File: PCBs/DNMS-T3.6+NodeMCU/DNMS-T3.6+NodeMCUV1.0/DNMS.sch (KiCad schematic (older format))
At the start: 12 parts, among them J1 Conn_2Rows-07Pins, J2 Conn_01x02, J3 Conn_01x04, J4 Conn_01x05, U1 NodeMCU V2, U2 NodeMCU V3, U3 Teensy3.6

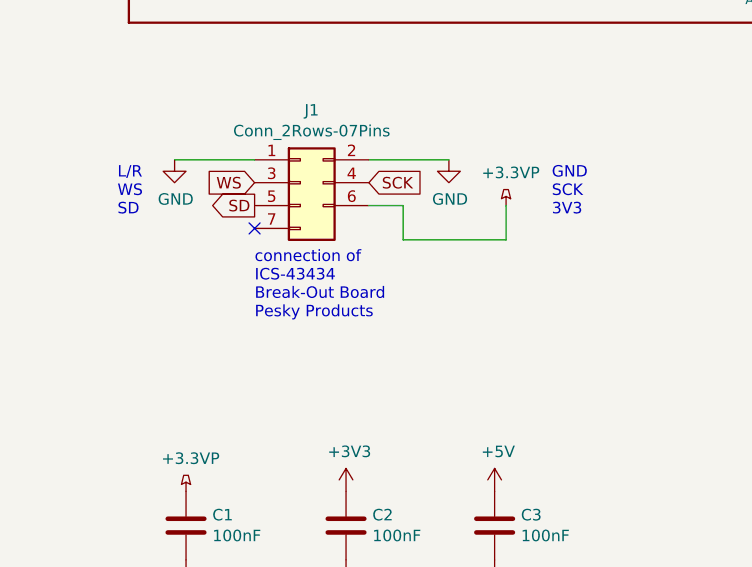
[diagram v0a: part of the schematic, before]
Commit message: spelling changes
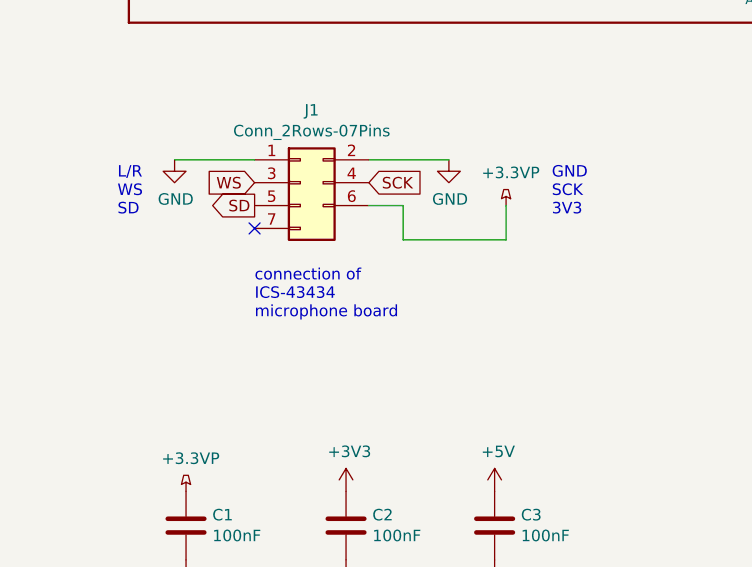
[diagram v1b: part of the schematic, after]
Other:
- note added: "connection of\nICS-43434\nmicrophone board"
- note removed: "connection of\nICS-43434\nBreak-Out Board\nPesky Products"
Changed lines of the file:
@@
 EESchema Schematic File Version 4
-LIBS:DNMS-cache
 EELAYER 30 0
 EELAYER END
@@
 L/R\nWS\nSD
 Text Notes 1950 5150 0    50   ~ 0
-connection of\nICS-43434\nBreak-Out Board\nPesky Products
+connection of\nICS-43434\nmicrophone board
 Text Notes 3250 4700 0    50   ~ 0
 GND\nSCK\n3V3
